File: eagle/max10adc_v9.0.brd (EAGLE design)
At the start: 98 x 62 mm, 206 parts, among them IC1 MAX19506, IC2 MAX19506, J1 MOLEX_BNC_73100-0105, J2 MOLEX_BNC_73100-0105, J3 MOLEX_BNC_73100-0105, J4 MOLEX_BNC_73100-0105, K1 AQY21SOP, K2 AQY21SOP, K3 AQY21SOP, K4 AQY21SOP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

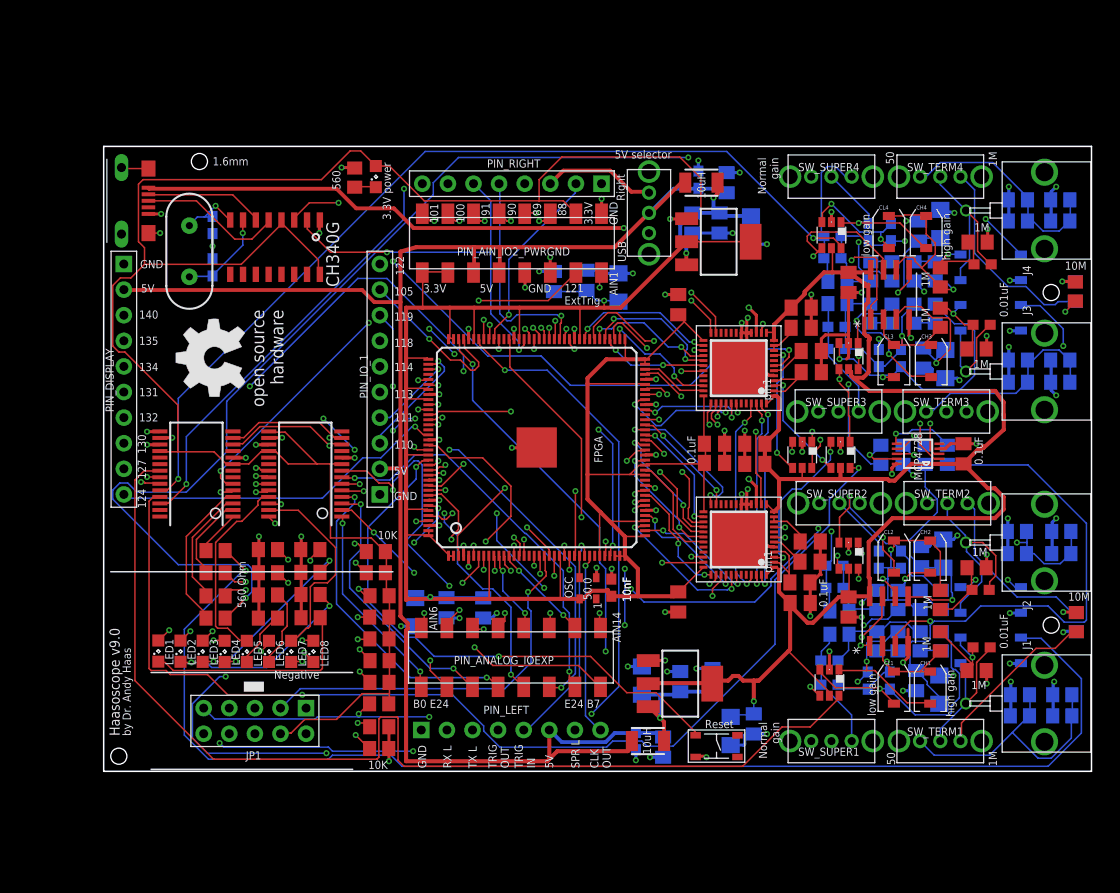
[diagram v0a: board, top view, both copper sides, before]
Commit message: v9, with 10M, 1.1M, and 11k input resistors, and rerouted
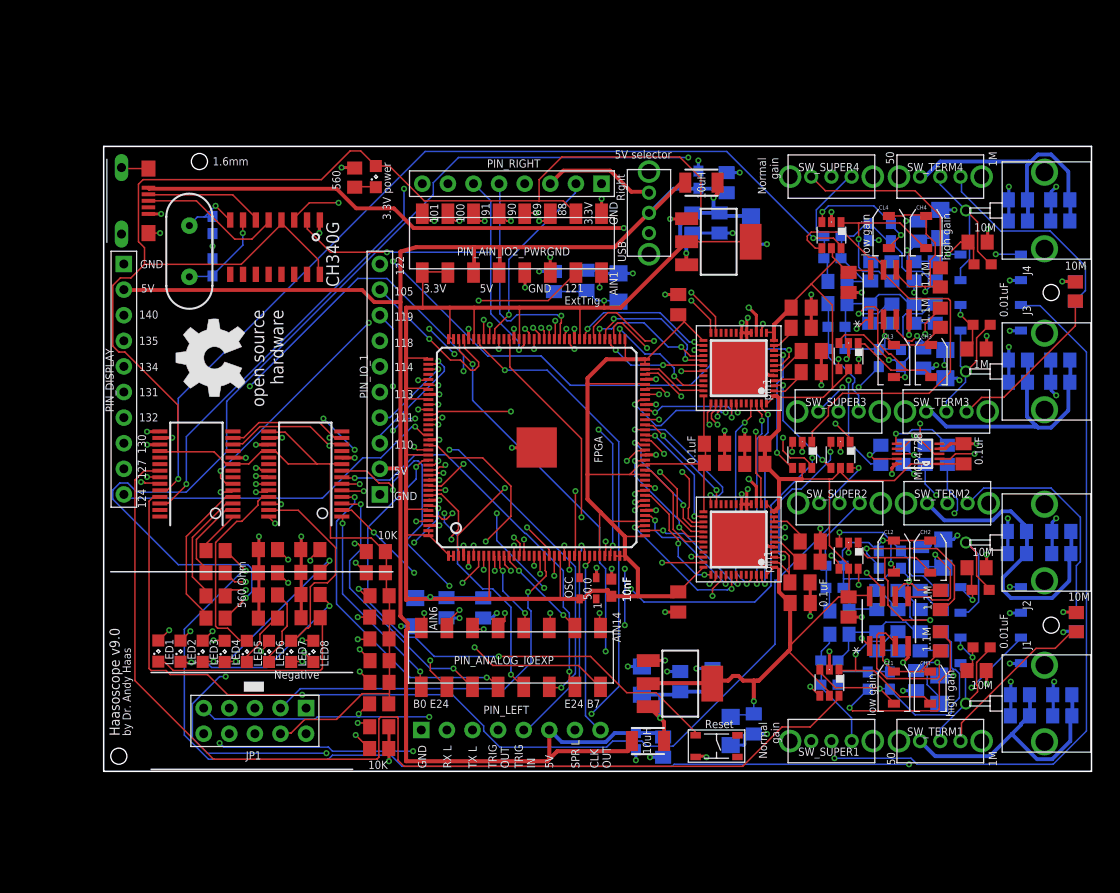
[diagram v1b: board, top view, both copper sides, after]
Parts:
- RIN1, RIN2, RIN3, RIN4: value 1M -> 1.1M
- RIN1_11K, RIN2_11K, RIN3_11K, RIN4_11K: value 10K -> 11K
- RIN5, RIN6, RIN7, RIN8: value 1M -> 10M
- renumbered RIN1_10K to RIN1_11K, RIN2_10K to RIN2_11K, RIN3_10K to RIN3_11K, RIN4_10K to RIN4_11K
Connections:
- removed net N$41: CIN5_4.2, C_AC4.1, K4.4, RIN4.1, RIN8.1, SW_SUPER4.2
- new net N$37: CIN5_1.1, RIN1.1, SW_SUPER1.1
- new net N$42: CIN5_3.1, RIN3.1, SW_SUPER3.1
- new net N$50: C_AC4.1, K4.4, RIN8.1, SW_SUPER4.2
- new net N$52: CIN5_4.1, RIN4.1, SW_SUPER4.1
- new net N$61: CIN5_2.1, RIN2.1, SW_SUPER2.1
- net INAMINUS1: now also CIN5_1.2; no longer CIN5_1.1
- net INAMINUS2: now also CIN5_3.2; no longer CIN5_3.1
- net INBMINUS1: now also CIN5_2.2; no longer CIN5_2.1
- net INBMINUS2: now also CIN5_4.2; no longer CIN5_4.1
- net N$10: no longer CIN5_1.2, RIN1.1
- net N$15: no longer CIN5_2.2, RIN2.1
- net N$39: no longer CIN5_3.2, RIN3.1
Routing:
- net VCCA: track 170.1 -> 134.7 mm
- net N$52: track 0.00 -> 29.9 mm, vias 0 -> 1
- net N$41: track 29.9 -> 0.00 mm, vias 1 -> 0
- net N$37: track 0.00 -> 25.4 mm, vias 0 -> 1
- net N$61: track 0.00 -> 23.6 mm, vias 0 -> 1
- net N$50: track 0.00 -> 21.0 mm, vias 0 -> 1
- net N$42: track 0.00 -> 20.0 mm, vias 0 -> 3
- net OFFSET1: track 59.0 -> 42.0 mm, vias 1 -> 2
- net N$11: track 127.0 -> 112.8 mm, vias 1 -> 3
- net GND: track 235.8 -> 222.9 mm, vias 98 -> 102
- net INA2: track 28.9 -> 16.0 mm, vias 2 -> 3
- net CGAIN4: track 10.8 -> 23.7 mm, vias 2 -> 1
- net INB2: track 32.7 -> 44.5 mm, vias 2 -> 0
- net N$32: track 147.1 -> 157.9 mm
- net N$25: track 21.3 -> 31.6 mm, vias 1 -> 0
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
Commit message: rotate osh logo
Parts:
- moved GOLD_ORB_SM1 4.56 mm to (2.60, 36.2), turned to 180 degrees
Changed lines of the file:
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@@
 <drawing>
 <settings>
-<setting alwaysvectorfont="no"/>
+<setting alwaysvectorfont="yes"/>
 <setting keepoldvectorfont="yes"/>
 <setting verticaltext="up"/>
@@
 <layers>
 <layer number="1" name="Top" color="4" fill="1" visible="yes" active="yes"/>
-<layer number="2" name="Route2" color="58" fill="10" visible="yes" active="yes"/>
+<layer number="2" name="Route2" color="58" fill="10" visible="no" active="yes"/>
 <layer number="3" name="Route3" color="4" fill="3" visible="no" active="no"/>
 <layer number="4" name="Route4" color="1" fill="4" visible="no" active="no"/>
@@
 <layer number="14" name="Route14" color="1" fill="6" visible="no" active="no"/>
 <layer number="15" name="Route15" color="13" fill="1" visible="yes" active="yes"/>
-<layer number="16" name="Bottom" color="1" fill="1" visible="yes" active="yes"/>
+<layer number="16" name="Bottom" color="1" fill="1" visible="no" active="yes"/>
 <layer number="17" name="Pads" color="2" fill="1" visible="yes" active="yes"/>
 <layer number="18" name="Vias" color="2" fill="1" visible="yes" active="yes"/>
@@
 <layer number="20" name="Dimension" color="15" fill="1" visible="yes" active="yes"/>
 <layer number="21" name="tPlace" color="7" fill="1" visible="yes" active="yes"/>
-<layer number="22" name="bPlace" color="7" fill="1" visible="yes" active="yes"/>
+<layer number="22" name="bPlace" color="7" fill="1" visible="no" active="yes"/>
 <layer number="23" name="tOrigins" color="15" fill="1" visible="yes" active="yes"/>
-<layer number="24" name="bOrigins" color="15" fill="1" visible="yes" active="yes"/>
+<layer number="24" name="bOrigins" color="15" fill="1" visible="no" active="yes"/>
 <layer number="25" name="tNames" color="7" fill="1" visible="yes" active="yes"/>
-<layer number="26" name="bNames" color="7" fill="1" visible="yes" active="yes"/>
+<layer number="26" name="bNames" color="7" fill="1" visible="no" active="yes"/>
 <layer number="27" name="tValues" color="7" fill="1" visible="yes" active="yes"/>
-<layer number="28" name="bValues" color="7" fill="1" visible="yes" active="yes"/>
+<layer number="28" name="bValues" color="7" fill="1" visible="no" active="yes"/>
 <layer number="29" name="tStop" color="7" fill="3" visible="no" active="yes"/>
 <layer number="30" name="bStop" color="7" fill="6" visible="no" active="yes"/>
@@
 <layer number="35" name="tGlue" color="7" fill="4" visible="no" active="yes"/>
 <layer number="36" name="bGlue" color="7" fill="5" visible="no" active="yes"/>
-<layer number="37" name="tTest" color="7" fill="1" visible="no" active="yes"/>
+<layer number="37" name="tTest" color="7" fill="1" visible="yes" active="yes"/>
 <layer number="38" name="bTest" color="7" fill="1" visible="no" active="yes"/>
 <layer number="39" name="tKeepout" color="4" fill="11" visible="yes" active="yes"/>
-<layer number="40" name="bKeepout" color="1" fill="11" visible="yes" active="yes"/>
+<layer number="40" name="bKeepout" color="1" fill="11" visible="no" active="yes"/>
 <layer number="41" name="tRestrict" color="4" fill="10" visible="yes" active="yes"/>
-<layer number="42" name="bRestrict" color="1" fill="10" visible="yes" active="yes"/>
+<layer number="42" name="bRestrict" color="1" fill="10" visible="no" active="yes"/>
 <layer number="43" name="vRestrict" color="2" fill="10" visible="no" active="yes"/>
 <layer number="44" name="Drills" color="7" fill="1" visible="no" active="yes"/>
@@
 <layer number="50" name="dxf" color="7" fill="1" visible="no" active="no"/>
 <layer number="51" name="tDocu" color="7" fill="1" visible="yes" active="yes"/>
-<layer number="52" name="bDocu" color="7" fill="1" visible="yes" active="yes"/>
+<layer number="52" name="bDocu" color="7" fill="1" visible="no" active="yes"/>
 <layer number="53" name="tGND_GNDA" color="7" fill="9" visible="no" active="no"/>
 <layer number="54" name="bGND_GNDA" color="1" fill="9" visible="no" active="no"/>
@@
 <attribute name="MPN" value="06035A560FAT2A" x="60.3" y="51.1" size="1.778" layer="28" rot="MR180" display="off"/>
 </element>
-<element name="GOLD_ORB_SM1" library="oshw" package="OSHW_8MM" value="OSHWLOGOLOGO8MM" x="-1" y="39" smashed="yes" rot="R90"/>
+<element name="GOLD_ORB_SM1" library="oshw" package="OSHW_8MM" value="OSHWLOGOLOGO8MM" x="2.6" y="36.2" smashed="yes" rot="R180"/>
 </elements>
 <signals>

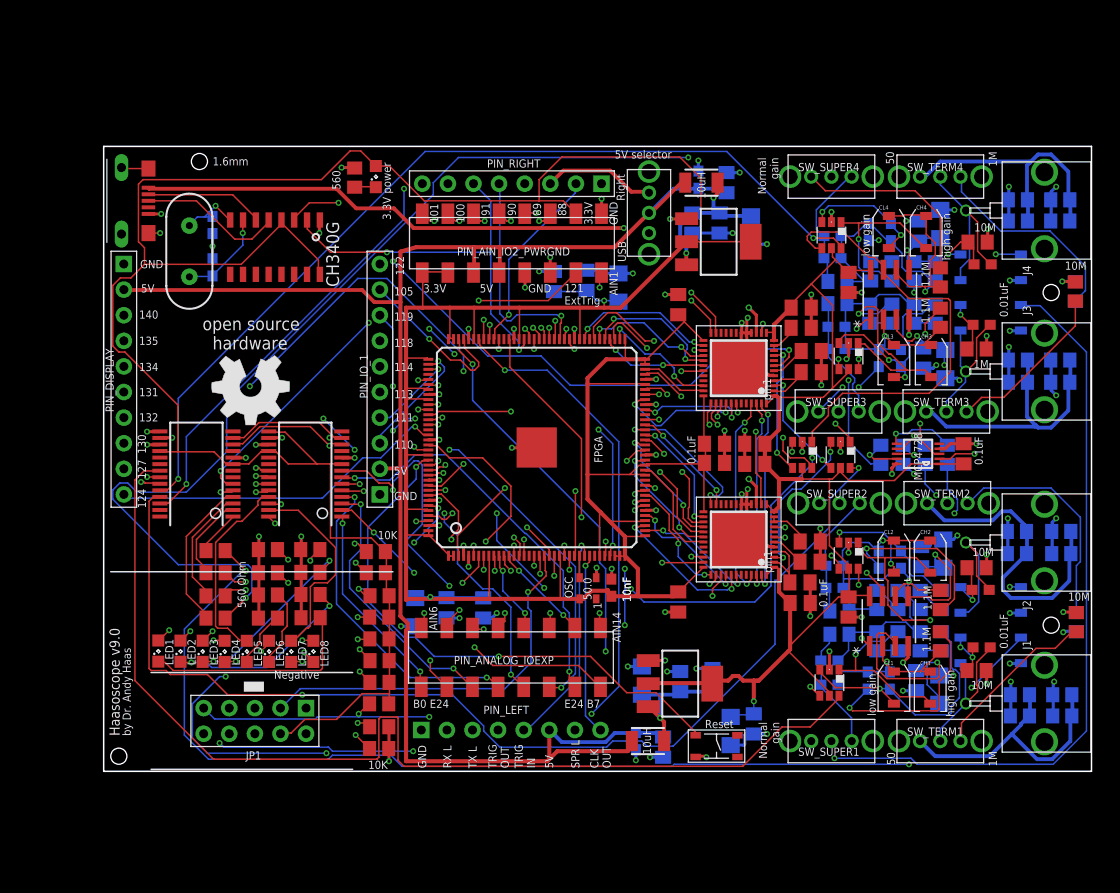
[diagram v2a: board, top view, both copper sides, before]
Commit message: updates for board 9.0 with dpdt switches
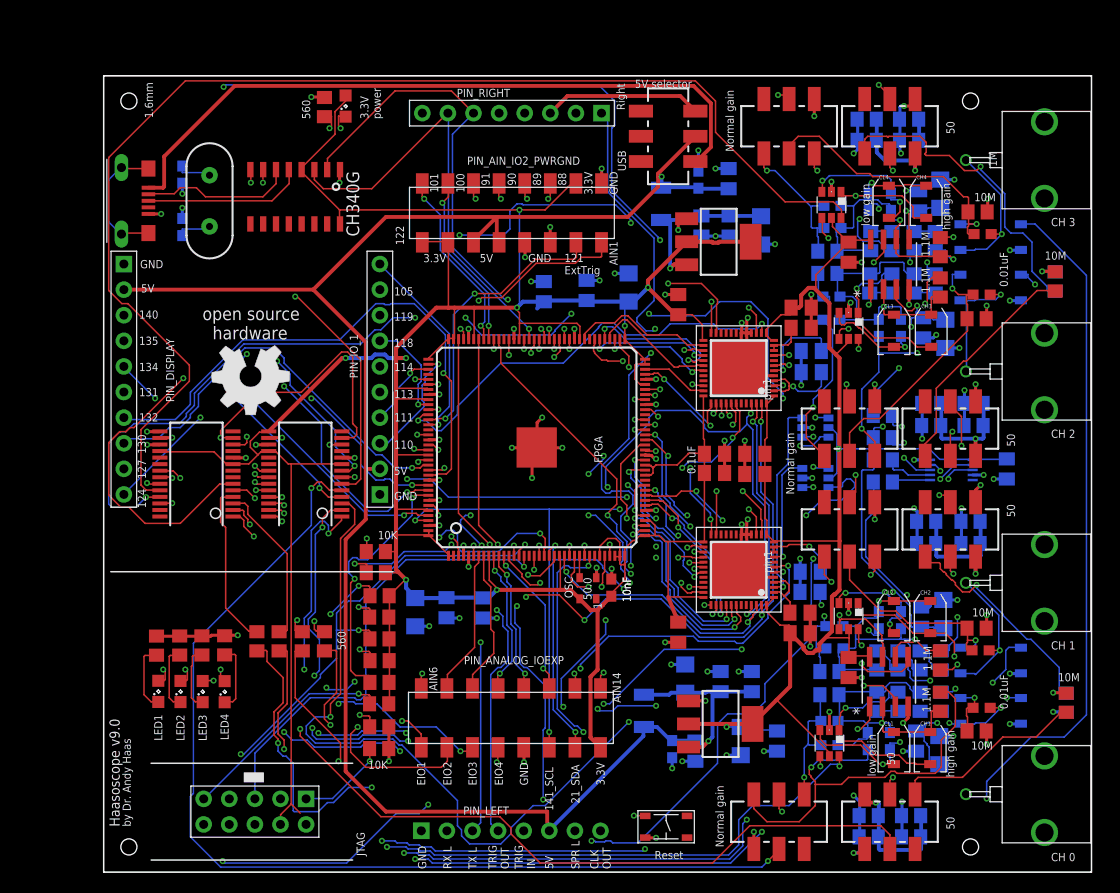
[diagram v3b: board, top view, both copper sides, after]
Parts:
- removed LED5, LED6, LED7, LED8: MF-LED-0805-RED, led:SML0805
- removed RLED5, RLED6, RLED7, RLED8: 560, resistor:R0805
- removed SW_5V, SW_SUPER1, SW_SUPER2, SW_SUPER3, SW_SUPER4, SW_TERM1, SW_TERM2, SW_TERM3, SW_TERM4: OS102011MS2QN1, PP_Electromechanical:0S102011MS2QS1
- added S1, S2, S3, S4, S5, S6, S7, S8, S9: JS202011SCQN, switch-ck:JS202011SCQN
- moved R50-1 19.2 mm to (63.9, -8.50)
- moved R50-2 19.2 mm to (63.9, -6.40)
- moved R50-3 19.2 mm to (68.1, -6.40)
- moved R50-4 19.2 mm to (68.1, -8.50)
- moved R50-13 17.0 mm to (63.7, 62.7)
- moved R50-14 17.0 mm to (63.7, 60.6)
- moved R50-15 17.0 mm to (67.9, 60.6)
- moved R50-16 17.0 mm to (67.9, 62.7)
- moved RLED1 15.5 mm to (-6.76, 10.5), turned to 90 degrees
- moved ACR1 14.1 mm to (9.90, 10.9), turned to 270 degrees
- moved RLED2 13.9 mm to (-4.46, 10.5), turned to 90 degrees
- moved RLED3 13.0 mm to (-2.26, 10.5), turned to 90 degrees
- moved RLED4 12.7 mm to (0.00, 10.5), turned to 90 degrees
- moved ACR2 11.0 mm to (7.70, 10.9), turned to 270 degrees
- moved PIN_LEFT 10.0 mm to (28.4, -7.90)
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- renumbered IOEXPAND_0X24_TOP to IOEXPAND_0X21_TOP
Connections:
- removed net DCLKA1: IC1.44
- removed net DCLKA2: IC2.44
- removed net DCLKB1: IC1.20
- removed net DCLKB2: IC2.20
- removed net DORA1: IC1.43
- removed net DORA2: IC2.43
- removed net DORB1: IC1.19
- removed net DORB2: IC2.19
- removed net E_24_B0: IOEXPAND_0X21_TOP.1, PIN_ANALOG_IOEXP.1
- removed net E_24_B1: IOEXPAND_0X21_TOP.2, PIN_ANALOG_IOEXP.3
- removed net E_24_B2: IOEXPAND_0X21_TOP.3, PIN_ANALOG_IOEXP.5
- removed net E_24_B3: IOEXPAND_0X21_TOP.4, PIN_ANALOG_IOEXP.7
- removed net E_24_B4: IOEXPAND_0X21_TOP.5, PIN_ANALOG_IOEXP.9
- removed net E_24_B5: IOEXPAND_0X21_TOP.6, PIN_ANALOG_IOEXP.11
- removed net E_24_B6: IOEXPAND_0X21_TOP.7, PIN_ANALOG_IOEXP.13
- removed net E_24_B7: IOEXPAND_0X21_TOP.8, PIN_ANALOG_IOEXP.15
- removed net LED5: IOEXPAND_0X21_TOP.25, LED5.A
- removed net LED6: IOEXPAND_0X21_TOP.26, LED6.A
- removed net LED7: IOEXPAND_0X21_TOP.27, LED7.A
- removed net LED8: IOEXPAND_0X21_TOP.28, LED8.A
- removed net N$16: LED6.C, RLED6.1
- removed net N$17: LED5.C, RLED5.1
- removed net N$38: CIN1NF_2.1, CIN56_2.1, RIN2_11K.1, SW_SUPER2.3
- removed net N$40: CIN1NF_3.1, CIN56_3.1, RIN3_11K.1, SW_SUPER3.3
- removed net N$42: CIN5_3.1, RIN3.1, SW_SUPER3.1
- removed net N$52: CIN5_4.1, RIN4.1, SW_SUPER4.1
- removed net N$53: CIN1NF_4.1, CIN56_4.1, RIN4_11K.1, SW_SUPER4.3
- removed net N$61: CIN5_2.1, RIN2.1, SW_SUPER2.1
- new net E_21_B0: IOEXPAND_0X21_TOP.1, S1.5
- new net E_21_B1: IOEXPAND_0X21_TOP.2, S2.5
- new net E_21_B2: IOEXPAND_0X21_TOP.3, S3.5
- new net E_21_B3: IOEXPAND_0X21_TOP.4, S4.5
- new net E_21_B4: IOEXPAND_0X21_TOP.5, S5.5
- new net E_21_B5: IOEXPAND_0X21_TOP.6, S6.5
- new net E_21_B6: IOEXPAND_0X21_TOP.7, S7.5
- new net E_21_B7: IOEXPAND_0X21_TOP.8, S8.5
- new net E_IO_1: IOEXPAND_0X21_TOP.25, PIN_ANALOG_IOEXP.1
- new net E_IO_2: IOEXPAND_0X21_TOP.26, PIN_ANALOG_IOEXP.3
- new net E_IO_3: IOEXPAND_0X21_TOP.27, PIN_ANALOG_IOEXP.5
- new net E_IO_4: IOEXPAND_0X21_TOP.28, PIN_ANALOG_IOEXP.7
- new net N$43: CIN1NF_3.1, CIN56_3.1, RIN3_11K.1, S7.1
- new net N$51: CIN5_3.1, RIN3.1, S7.3
- new net N$56: CIN1NF_4.1, CIN56_4.1, RIN4_11K.1, S8.1
- new net N$57: CIN5_4.1, RIN4.1, S8.3
- net +3V3: now also PIN_ANALOG_IOEXP.15
- net +5V: now also S9.2; no longer SW_5V.2
- net 5VINFROMRIGHT: now also S9.3; no longer SW_5V.3
- net 5VINFROMUSB: now also S9.1; no longer SW_5V.1
- net GND: now also PIN_ANALOG_IOEXP.9, S1.6, S2.6, S3.6, S4.6, S5.6, S6.6, S7.6, S8.6; no longer RLED5.2, RLED6.2, RLED7.2, RLED8.2
- net INJ1: now also S1.2; no longer SW_TERM1.2
- net INJ2: now also S2.2; no longer SW_TERM2.2
- net INJ3: now also S3.2; no longer SW_TERM3.2
- net INJ4: now also S4.2; no longer SW_TERM4.2
- net L141_SCL: now also PIN_ANALOG_IOEXP.11
- net L21_SDA: now also PIN_ANALOG_IOEXP.13
- net N$10: now also S5.2; no longer SW_SUPER1.2
- net N$15: now also S6.2; no longer SW_SUPER2.2
- net N$19: now also CIN1NF_2.1, CIN56_2.1, RIN2_11K.1, S6.1; no longer LED7.C, RLED7.1
- net N$20: now also S5.1; no longer SW_SUPER1.3
- net N$22: now also CIN5_2.1, RIN2.1, S6.3; no longer LED8.C, RLED8.1
- net N$24: now also S1.1; no longer SW_TERM1.3
- net N$25: now also S2.3; no longer SW_TERM2.1
- net N$26: now also S3.3; no longer SW_TERM3.1
- net N$27: now also S2.1; no longer SW_TERM2.3
- net N$28: now also S4.3; no longer SW_TERM4.1
- net N$29: now also S1.3; no longer SW_TERM1.1
- net N$30: now also S3.1; no longer SW_TERM3.3
- net N$33: now also S4.1; no longer SW_TERM4.3
- net N$37: now also S5.3; no longer SW_SUPER1.1
- net N$39: now also S7.2; no longer SW_SUPER3.2
- net N$50: now also S8.2; no longer SW_SUPER4.2
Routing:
- net E_21_B5: track 0.00 -> 135.5 mm, vias 0 -> 2
- net E_21_B2: track 0.00 -> 123.7 mm, vias 0 -> 3
- net E_21_B1: track 0.00 -> 105.2 mm, vias 0 -> 7
- net E_21_B4: track 0.00 -> 103.6 mm, vias 0 -> 2
- net E_21_B3: track 0.00 -> 99.1 mm, vias 0 -> 3
- net E_21_B0: track 0.00 -> 93.8 mm, vias 0 -> 3
- net E_21_B7: track 0.00 -> 80.2 mm, vias 0 -> 3
- net E_21_B6: track 0.00 -> 70.9 mm, vias 0 -> 4
- net +3V3: track 437.3 -> 382.3 mm, vias 2 -> 8
- net GND: track 222.9 -> 273.7 mm, vias 102 -> 117
- net E_IO_4: track 0.00 -> 47.0 mm, vias 0 -> 2
- net E_SHDN2: track 81.8 -> 128.5 mm
- net E_24_B7: track 46.4 -> 0.00 mm, vias 3 -> 0
- net E_24_B5: track 45.2 -> 0.00 mm, vias 3 -> 0
- net E_IO_2: track 0.00 -> 43.8 mm, vias 0 -> 2
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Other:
- board size 98 x 62 mm -> 98 x 79 mm
- board text added: "141_SCL"
- board text added: "21_SDA"
- board text added: "CH 0"
- board text added: "CH 1"
- board text added: "CH 2"
- board text added: "CH 3"
- board text added: "EIO1"
- board text added: "EIO2"
- board text added: "EIO3"
- board text added: "EIO4"
- board text added: "JTAG"
- board text removed: "560 Ohm"
- board text removed: "B0 E24"
- board text removed: "E24 B7"
- board text removed: "Negative"
